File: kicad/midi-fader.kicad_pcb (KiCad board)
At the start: 2 copper layers, 73.7 x 78.7 mm, 101 parts, among them J1 SWD, J2 EXTERNAL_OUT, J3 EXTERNAL_IN, J4 USB_OTG, U1 STM32F042KxT, U2 USBLC6-2, U3 MCP1603, U4 MIC2776L, U5 MIC5501-XYM5

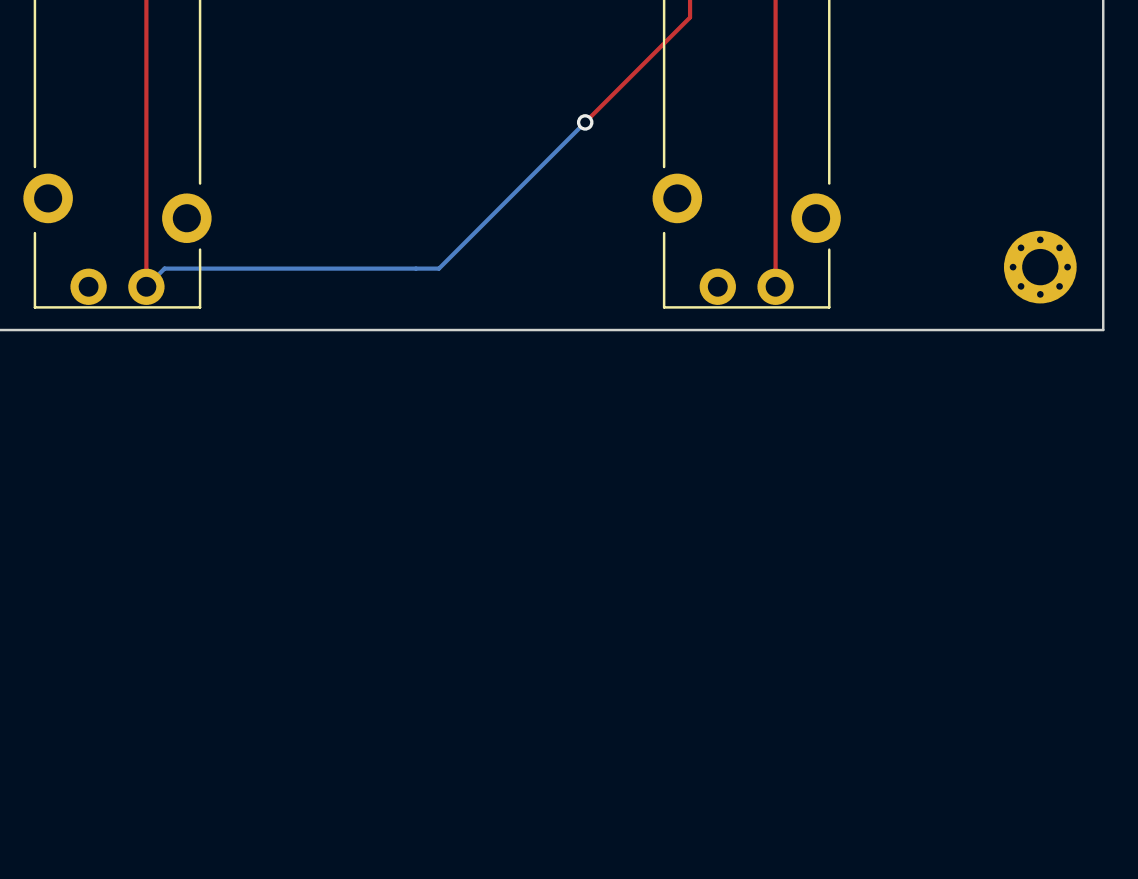
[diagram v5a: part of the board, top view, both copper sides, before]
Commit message: Created shift register circuitry and imported footprints
I think 5MHz to 10MHz is the theoretical maximum of this circuit. Actual
frequency will probably be around 5MHz or somewhat less given the signal
integrity issues on a 2-layer board with this many plane breaks.

Created footprints for button and HTSSOP

The HTSSOP footprint is special because I plan to hand solder, so I
added excessive thermal vias and a bare pad on the backside.

The netlist is imported to the PCB, but only the switches are placed.
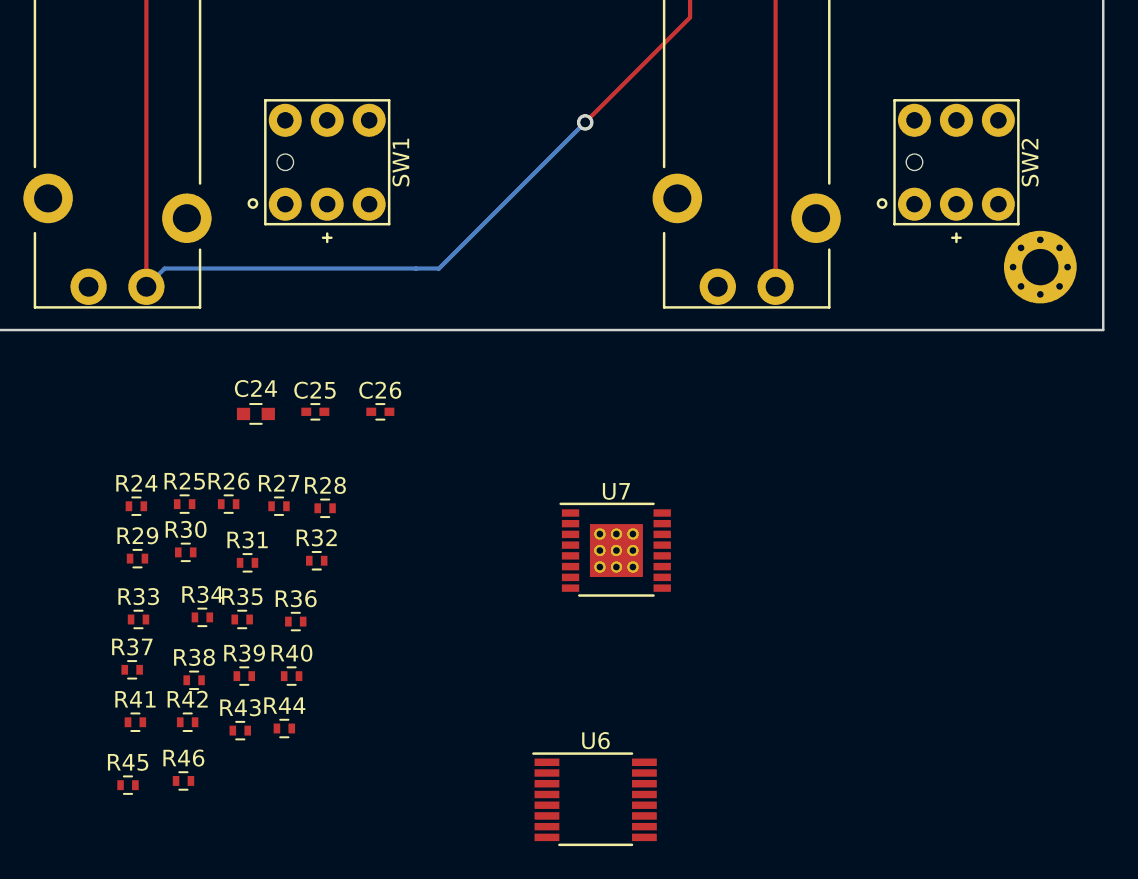
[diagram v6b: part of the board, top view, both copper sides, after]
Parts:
- added C24: 1u, Capacitors_SMD:C_0603, F.Cu at (139.2, 147.3)
- added C25: 0.1u, Capacitors_SMD:C_0402, F.Cu at (142.8, 147.2)
- added C26: 0.1u, Capacitors_SMD:C_0402, F.Cu at (146.7, 147.2)
- added R24: 33, Resistors_SMD:R_0402, F.Cu at (132.0, 152.9)
- added R25: 33, Resistors_SMD:R_0402, F.Cu at (134.9, 152.8)
- added R26: 33, Resistors_SMD:R_0402, F.Cu at (137.5, 152.8)
- added R27: 33, Resistors_SMD:R_0402, F.Cu at (140.6, 152.9)
- added R28: 10K, Resistors_SMD:R_0402, F.Cu at (143.4, 153.0)
- added R29: 10K, Resistors_SMD:R_0402, F.Cu at (132.0, 156.1)
- added R30: 10K, Resistors_SMD:R_0402, F.Cu at (134.9, 155.7)
- added R31: 10K, Resistors_SMD:R_0402, F.Cu at (138.7, 156.3)
- added R32: 10K, Resistors_SMD:R_0402, F.Cu at (142.9, 156.2)
- added R33: 10K, Resistors_SMD:R_0402, F.Cu at (132.1, 159.8)
- added R34: 10K, Resistors_SMD:R_0402, F.Cu at (135.9, 159.6)
- added R35: 10K, Resistors_SMD:R_0402, F.Cu at (138.4, 159.8)
- added R36: 10K, Resistors_SMD:R_0402, F.Cu at (141.6, 159.9)
- added R37: 0, Resistors_SMD:R_0402, F.Cu at (131.7, 162.8)
- added R38: 33, Resistors_SMD:R_0402, F.Cu at (135.5, 163.4)
- added R39: SPR, Resistors_SMD:R_0402, F.Cu at (138.5, 163.2)
- added R40: 10K, Resistors_SMD:R_0402, F.Cu at (141.4, 163.2)
- added R41: 0, Resistors_SMD:R_0402, F.Cu at (131.9, 166.0)
- added R42: 33, Resistors_SMD:R_0402, F.Cu at (135.1, 166.0)
- added R43: SPR, Resistors_SMD:R_0402, F.Cu at (138.2, 166.5)
- added R44: 2K2, Resistors_SMD:R_0402, F.Cu at (140.9, 166.4)
- added R45: 0, Resistors_SMD:R_0402, F.Cu at (131.4, 169.8)
- added R46: 0, Resistors_SMD:R_0402, F.Cu at (134.8, 169.5)
- added SW1: TR2-21-L5, midi-fader:Nidec_Copal_TR2, F.Cu at (143.5, 132.1)
- added SW2: TR2-21-L5, midi-fader:Nidec_Copal_TR2, F.Cu at (181.6, 132.1)
- added U6: 74HC165, Housings_SSOP:TSSOP-16_4.4x5mm_Pitch0.65mm, F.Cu at (159.8, 170.7)
- added U7: STP08DP05, midi-fader:HTSSOP-16-1EP_4.4x5mm_Pitch0.65mm_ThermalVias_HandSolder, F.Cu at (161.0, 155.6)
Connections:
- J2 pad 13: Net-(J2-Pad13) -> /Input/LCLK_STUB
- J2 pad 14: Net-(J2-Pad14) -> /Input/SCLK_STUB
- J2 pad 4: Net-(J2-Pad4) -> /Input/LED_IN
- J2 pad 5: Net-(J2-Pad5) -> /Digital Control/~OE
- J2 pad 6: Net-(J2-Pad6) -> /Input/BTN_OUT
- J3 pad 13: Net-(J3-Pad13) -> /Digital Control/LCLK
- J3 pad 14: Net-(J3-Pad14) -> /Digital Control/SCLK
- J3 pad 4: Net-(J3-Pad4) -> /Input/LED_OUT
- J3 pad 5: Net-(J3-Pad5) -> /Digital Control/~OE
- J3 pad 6: Net-(J3-Pad6) -> /Input/BTN_IN
- U1 pad 14: Net-(U1-Pad14) -> /Digital Control/LCLK_R
- U1 pad 15: Net-(U1-Pad15) -> /Digital Control/~OE_R
- U1 pad 26: Net-(U1-Pad26) -> /Digital Control/SCLK_R
- U1 pad 27: Net-(U1-Pad27) -> /Digital Control/MISO
- U1 pad 28: Net-(U1-Pad28) -> /Digital Control/MOSI_R

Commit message: Layout completed, first pass
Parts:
- added REF**: 1PIN_VIA, midi-fader:1PIN_VIA, F.Cu at (180.6, 109.6)
- added REF**: 1PIN_VIA, midi-fader:1PIN_VIA, F.Cu at (143.3, 110.5)
- added REF**: 1PIN_VIA, midi-fader:1PIN_VIA, F.Cu at (145.4, 114.9)
- added REF**: 1PIN_VIA, midi-fader:1PIN_VIA, F.Cu at (145.4, 114.2)
- added REF**: 1PIN_VIA, midi-fader:1PIN_VIA, F.Cu at (149.0, 116.7)
- added REF**: 1PIN_VIA, midi-fader:1PIN_VIA, F.Cu at (133.5, 116.7)
- added REF**: 1PIN_VIA, midi-fader:1PIN_VIA, F.Cu at (127.1, 112.4)
- added REF**: 1PIN_VIA, midi-fader:1PIN_VIA, F.Cu at (127.1, 111.5)
- added REF**: 1PIN_VIA, midi-fader:1PIN_VIA, F.Cu at (127.1, 110.6)
- added REF**: 1PIN_VIA, midi-fader:1PIN_VIA, F.Cu at (127.1, 109.7)
- added REF**: 1PIN_VIA, midi-fader:1PIN_VIA, F.Cu at (131.6, 112.5)
- added REF**: 1PIN_VIA, midi-fader:1PIN_VIA, F.Cu at (181.4, 108.8)
- added REF**: 1PIN_VIA, midi-fader:1PIN_VIA, F.Cu at (131.4, 111.5)
- added REF**: 1PIN_VIA, midi-fader:1PIN_VIA, F.Cu at (131.3, 110.5)
- added REF**: 1PIN_VIA, midi-fader:1PIN_VIA, F.Cu at (130.7, 109.7)
- added REF**: 1PIN_VIA, midi-fader:1PIN_VIA, F.Cu at (125.2, 112.4)
- added REF**: 1PIN_VIA, midi-fader:1PIN_VIA, F.Cu at (125.2, 111.5)
- added REF**: 1PIN_VIA, midi-fader:1PIN_VIA, F.Cu at (125.2, 110.6)
- added REF**: 1PIN_VIA, midi-fader:1PIN_VIA, F.Cu at (125.2, 109.7)
- added REF**: 1PIN_VIA, midi-fader:1PIN_VIA, F.Cu at (125.3, 100.7)
- added REF**: 1PIN_VIA, midi-fader:1PIN_VIA, F.Cu at (123.3, 93.0)
- added REF**: 1PIN_VIA, midi-fader:1PIN_VIA, F.Cu at (152.8, 112.0)
- added REF**: 1PIN_VIA, midi-fader:1PIN_VIA, F.Cu at (182.1, 108.1)
- added REF**: 1PIN_VIA, midi-fader:1PIN_VIA, F.Cu at (154.7, 113.2)
- added REF**: 1PIN_VIA, midi-fader:1PIN_VIA, F.Cu at (152.7, 109.0)
- added REF**: 1PIN_VIA, midi-fader:1PIN_VIA, F.Cu at (153.5, 109.0)
- added REF**: 1PIN_VIA, midi-fader:1PIN_VIA, F.Cu at (173.0, 110.2)
- added REF**: 1PIN_VIA, midi-fader:1PIN_VIA, F.Cu at (174.2, 110.2)
- added REF**: 1PIN_VIA, midi-fader:1PIN_VIA, F.Cu at (175.4, 110.2)
- added REF**: 1PIN_VIA, midi-fader:1PIN_VIA, F.Cu at (138.9, 118.6)
- added REF**: 1PIN_VIA, midi-fader:1PIN_VIA, F.Cu at (136.8, 118.6)
- added REF**: 1PIN_VIA, midi-fader:1PIN_VIA, F.Cu at (134.5, 118.6)
- C26, R24, R25, R37, R38, R40, R44, R45, R46, U6: moved to B.Cu
- moved R26 78.4 mm to (156.8, 76.8), turned to 270 degrees
- moved R27 78.2 mm to (158.8, 76.8), turned to 270 degrees
- moved R24 69.9 mm to (158.9, 88.4), turned to 270 degrees
- moved R25 68.3 mm to (157.6, 88.4), turned to 270 degrees
- moved R42 63.9 mm to (157.1, 106.0), turned to 90 degrees
- moved R44 62.4 mm to (156.5, 105.9), turned to 90 degrees
- moved U6 60.6 mm to (148.7, 111.1), turned to 90 degrees
- moved R37 60.4 mm to (145.9, 104.1)
- moved R39 60.2 mm to (152.5, 104.6), turned to 90 degrees
- moved R40 58.7 mm to (152.5, 105.5), turned to 90 degrees
- moved R38 58.5 mm to (145.4, 105.8), turned to 90 degrees
- moved R45 56.9 mm to (150.2, 116.1), turned to 180 degrees
- moved R41 55.4 mm to (155.2, 115.7), turned to 180 degrees
- moved R46 54.4 mm to (150.2, 117.3)
- moved R29 53.7 mm to (147.4, 104.6), turned to 270 degrees
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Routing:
- net /Digital Control/SCLK: track 0.00 -> 126.4 mm, vias 0 -> 7
- net /Digital Control/LCLK: track 0.00 -> 98.8 mm, vias 0 -> 7
- net /Digital Control/~OE: track 0.00 -> 92.5 mm, vias 0 -> 7
- net VDD: track 0.00 -> 88.9 mm, vias 0 -> 5
- net /Input/BTN1: track 0.00 -> 88.1 mm, vias 0 -> 8
- net /Input/BTN_IN: track 0.00 -> 79.3 mm, vias 0 -> 5
- net /Input/LCLK_STUB: track 0.00 -> 56.1 mm, vias 0 -> 1
- net /Digital Control/MOSI: track 0.00 -> 51.5 mm, vias 0 -> 4
- net /Input/SCLK_STUB: track 0.00 -> 50.0 mm, vias 0 -> 1
- net /Input/LED1: track 0.00 -> 47.8 mm, vias 0 -> 2
- net /Input/LED_IN: track 0.00 -> 47.0 mm, vias 0 -> 2
- net /Input/BTN0: track 0.00 -> 45.9 mm, vias 0 -> 4
- net /Digital Control/MISO: track 0.00 -> 41.7 mm, vias 0 -> 2
- net /Input/LED_OUT: track 0.00 -> 33.3 mm, vias 0 -> 6
- net /Input/BTN_OUT: track 0.00 -> 31.2 mm, vias 0 -> 2
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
